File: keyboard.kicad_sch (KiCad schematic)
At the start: 29 parts, among them SW1 F1, SW10 4, SW11 9, SW12 5, SW13 A, SW14 6, SW15 B, SW16 7, SW17 0, SW18 INC, SW19 1, SW2 F2, SW20 DEC, SW21 2, SW22 SEL, SW23 3, SW24 GO!, SW3 F3, SW4 F4, SW5 C, SW6 D, SW7 E, SW8 F, SW9 8, U2 74HC244

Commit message: HW: Update schematic info frames
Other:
- company: (none) -> A.K.
- title: (none) -> Matrix keyboard
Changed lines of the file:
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@@
 	(generator_version "9.0")
 	(paper "A4")
+	(title_block
+		(title "Matrix keyboard")
+		(date "2025-10-14")
+		(rev "A")
+		(company "A.K.")
+	)
 	(junction
 		(at 118.11 104.14)

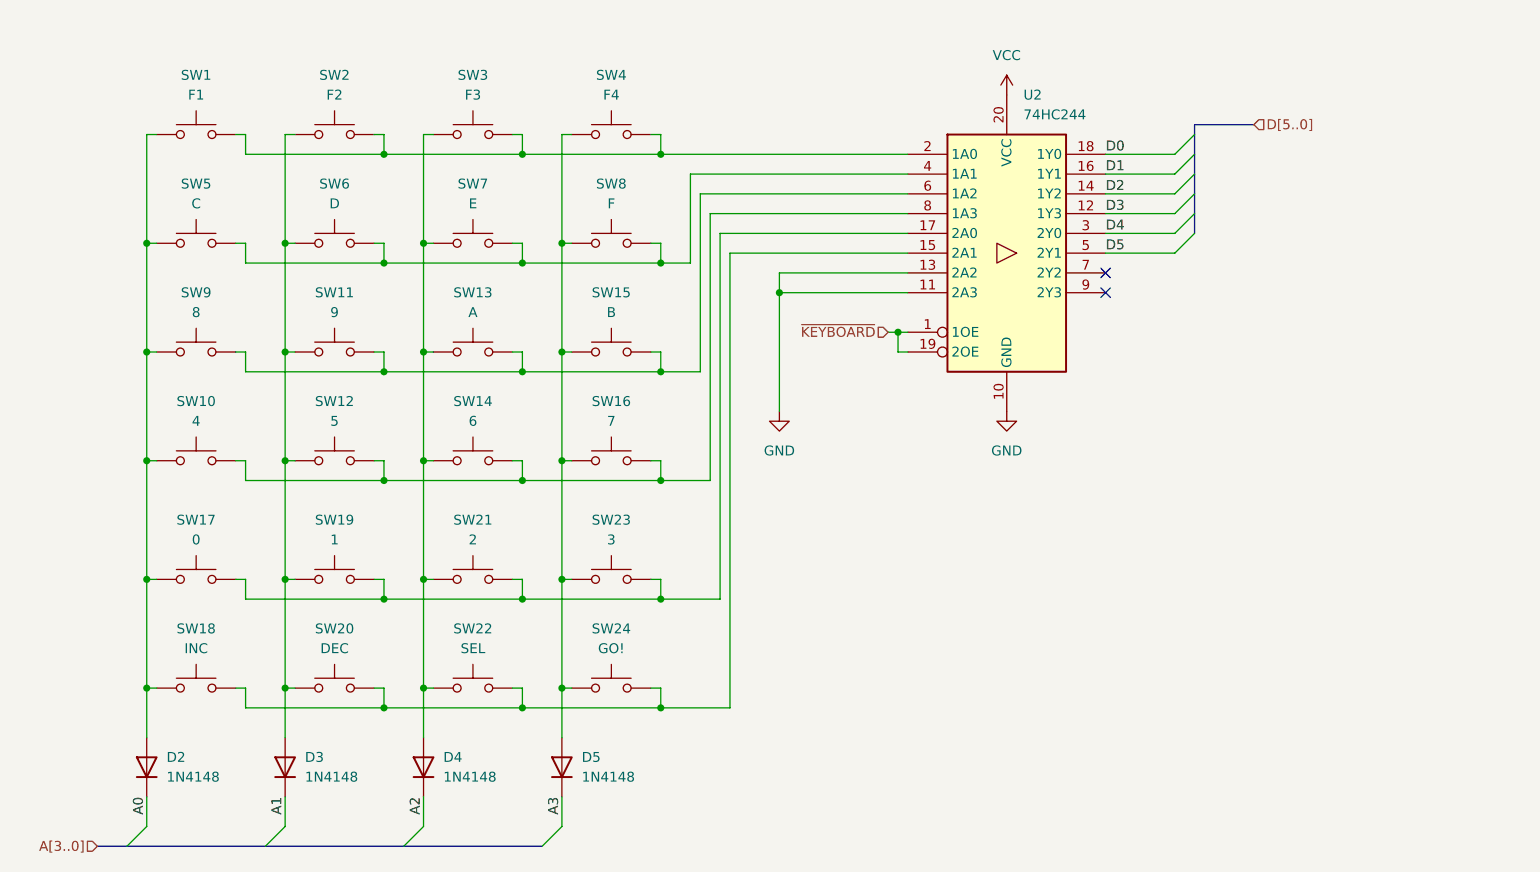
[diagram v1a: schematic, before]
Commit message: HW: Add display, start PCB placement
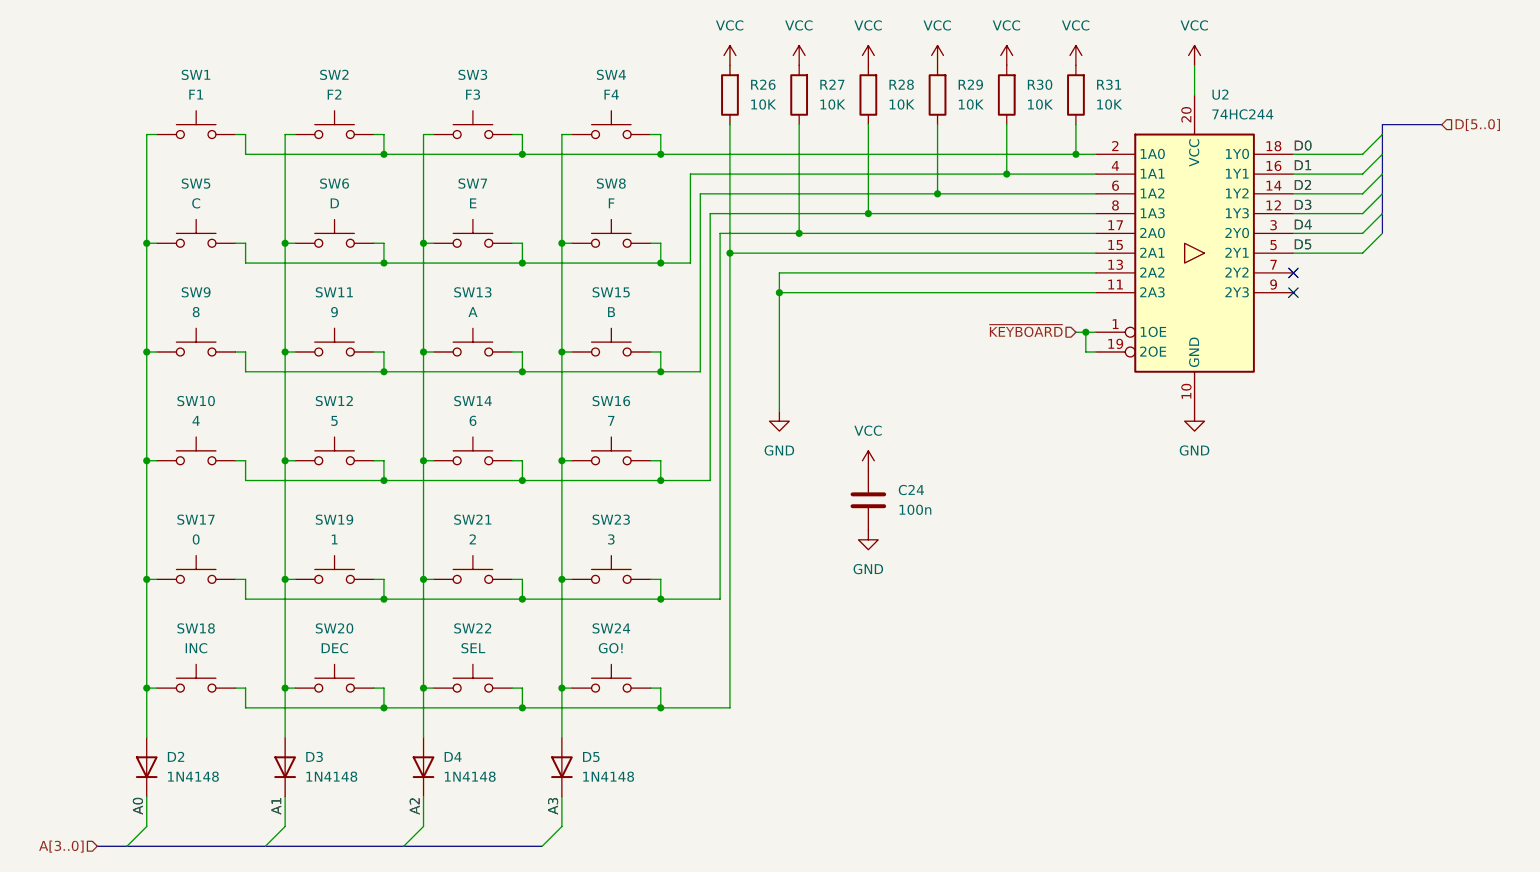
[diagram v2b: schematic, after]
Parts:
- added C24: 100n, Capacitor_SMD:C_0805_2012Metric, symbol Device:C
- added R26, R27, R28, R29, R30, R31: 10K, Resistor_SMD:R_0805_2012Metric, symbol Device:R
- SW1, SW10, SW11, SW12, SW13, SW14, SW15, SW16, SW17, SW18, SW19, SW2, SW20, SW21, SW22, SW23, SW24, SW3, SW4, SW5, SW6, SW7, SW8, SW9: footprint Button_Switch_SMD:SW_SPST_PTS647_Sx38 -> Button_Switch_SMD:SW_SPST_PTS645
- U2: footprint (none) -> Package_SO:SOIC-20W_7.5x12.8mm_P1.27mm
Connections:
- net GND: now also C24.2
- net VCC: now also C24.1, R26.2, R27.2, R28.2, R29.2, R30.2, R31.2
- net at SW10.2, SW12.2, SW14.2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: now also R28.1
- net at SW1.2, SW2.2, SW3.2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: now also R31.1
- net at SW5.2, SW6.2, SW7.2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: now also R30.1
- net at SW17.2, SW19.2, SW21.2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: now also R27.1
- net at SW18.2, SW20.2, SW22.2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: now also R26.1
- net at SW11.2, SW13.2, SW15.2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: now also R29.1
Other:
- moved on the sheet: U2

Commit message: HW: Start final placement
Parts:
- D3, D4, D5: footprint Diode_SMD:D_MicroMELF -> Diode_SMD:D_MiniMELF
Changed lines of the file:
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@@
 			)
 		)
-		(property "Footprint" "Diode_SMD:D_MicroMELF"
+		(property "Footprint" "Diode_SMD:D_MiniMELF"
 			(at 135.89 143.51 0)
 			(effects
@@
 			)
 		)
-		(property "Footprint" "Diode_SMD:D_MicroMELF"
+		(property "Footprint" "Diode_SMD:D_MiniMELF"
 			(at 118.11 143.51 0)
 			(effects
@@
 			)
 		)
-		(property "Footprint" "Diode_SMD:D_MicroMELF"
+		(property "Footprint" "Diode_SMD:D_MiniMELF"
 			(at 100.33 143.51 0)
 			(effects

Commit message: HW: placement finished
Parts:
- D2: footprint Diode_SMD:D_MicroMELF -> Diode_SMD:D_MiniMELF
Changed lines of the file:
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@@
 			)
 		)
-		(property "Footprint" "Diode_SMD:D_MicroMELF"
+		(property "Footprint" "Diode_SMD:D_MiniMELF"
 			(at 82.55 143.51 0)
 			(effects
